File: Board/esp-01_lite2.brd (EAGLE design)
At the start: 13.5 x 60 mm, 27 parts, among them IC1 TINY13-20SU

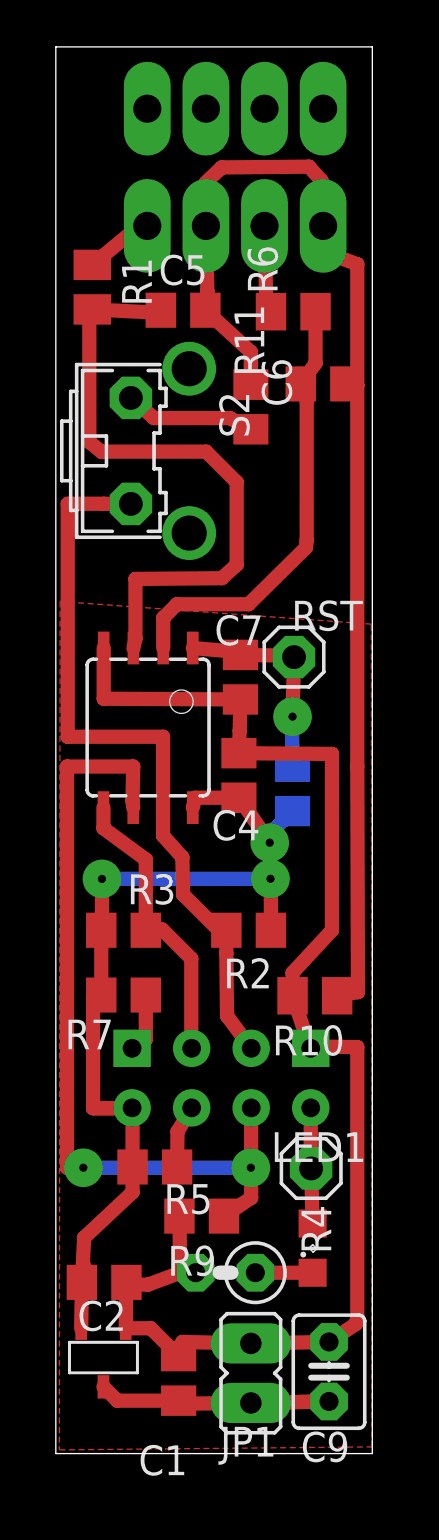
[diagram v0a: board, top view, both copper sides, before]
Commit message: v0.4 remove capacitor
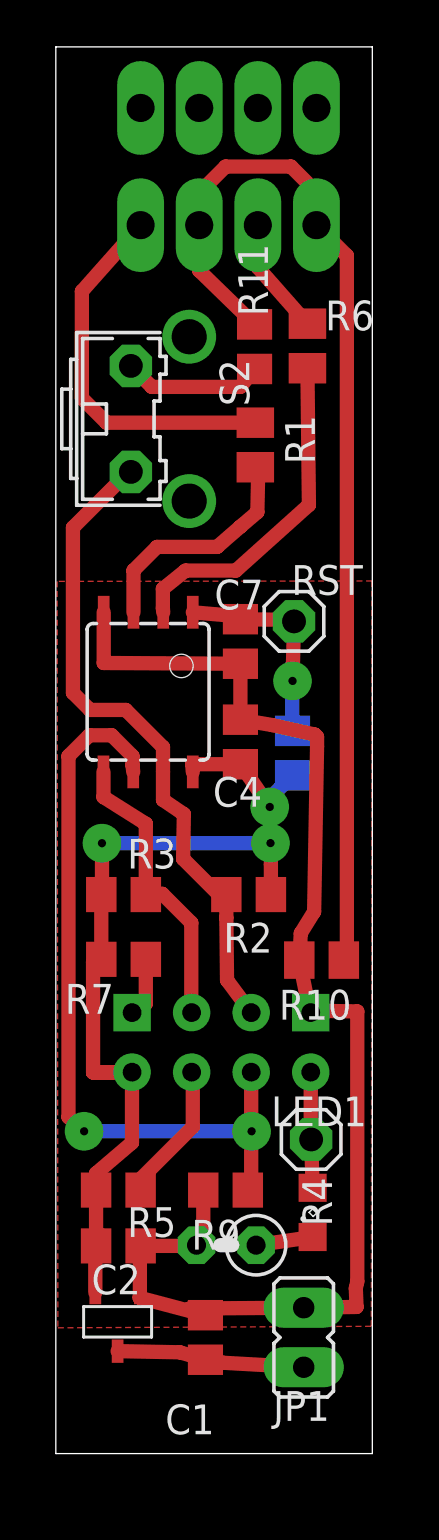
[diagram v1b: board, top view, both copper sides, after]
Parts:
- removed C5, C6: 0.47, resistor:C0805
- removed C9: 10mkF, rcl:C025-030X050
- moved R1 9.68 mm to (8.51, 43.0)
- moved JP1 2.72 mm to (10.6, 4.95)
- moved R11 2.58 mm to (8.48, 47.2)
- moved C1 2.09 mm to (6.38, 4.95)
- moved R5 1.84 mm to (2.67, 11.2)
- moved C2 1.67 mm to (2.67, 8.86)
- moved U$2 1.64 mm to (2.64, 5.62)
- moved R6 1.58 mm to (10.7, 47.2), turned to 270 degrees
- moved R10 1.55 mm to (11.3, 21.1)
- moved LED1 1.52 mm to (11.0, 10.3)
- moved R7 1.52 mm to (2.89, 21.1)
- moved R8 1.52 mm to (10.1, 29.9)
- moved RST 1.52 mm to (10.2, 35.5)
- moved U$1 1.52 mm to (7.05, 24.4)
- moved IC1 1.52 mm to (3.94, 32.5)
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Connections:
- net AA*3: no longer C9.1
- net GND: no longer C9.2
- net GND1: no longer C5.1, C6.1
- net IN1: no longer C6.2
- net IN2: no longer C5.2
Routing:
- net IN2: track 27.1 -> 10.0 mm
- net N$4: track 2.98 -> 16.2 mm
- net GND1: track 53.4 -> 45.8 mm
- net AA*3: track 13.2 -> 8.00 mm
- net IN1: track 19.1 -> 14.4 mm
- net N$11: track 2.69 -> 5.97 mm
- net SCK: track 31.6 -> 28.4 mm
- net WAKE_UP: track 34.8 -> 32.8 mm
- net GND: track 60.2 -> 58.3 mm
- net N$3: track 3.69 -> 5.00 mm
